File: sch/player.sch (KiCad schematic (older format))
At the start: 74 parts, among them J4 USB_B, U4 CC1101

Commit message: mic add, rf433
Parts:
- removed C28: 1pF, Capacitor_SMD:C_0603_1608Metric_Pad1.05x0.95mm_HandSolder, symbol Device:C
- removed C32: 12pF, Capacitor_SMD:C_0603_1608Metric_Pad1.05x0.95mm_HandSolder, symbol Device:C
- removed C34: 47pF, Capacitor_SMD:C_0603_1608Metric_Pad1.05x0.95mm_HandSolder, symbol Device:C
- removed C?: 220p, symbol Device:C
- removed C?: 10uF, Capacitor_SMD:C_0805_2012Metric, symbol Device:C
- removed D?: 1N5822, Diode_SMD:D_SMA, symbol Diode:1N5822
- removed L1, L2: 12nH, Inductor_SMD:L_0603_1608Metric_Pad1.05x0.95mm_HandSolder, symbol Device:L
- removed L7: 3.3nH, Inductor_SMD:L_0603_1608Metric_Pad1.05x0.95mm_HandSolder, symbol Device:L
- removed R?: 1, symbol Device:R
- removed R?: 18k, symbol Device:R
- removed R?: 11k, symbol Device:R
- removed U?: MC33063AD, Package_SO:SOIC-8_3.9x4.9mm_P1.27mm, symbol Regulator_Switching:MC33063AD
- added BT?: AAA_Cell, symbol Device:Battery_Cell
- added C? (x2): 10uF, Capacitor_SMD:C_0805_2012Metric, symbol Device:C
- added C? (x2): 1uF, Capacitor_SMD:C_0805_2012Metric, symbol Device:C
- added C?: 12pF, Capacitor_SMD:C_0603_1608Metric_Pad1.05x0.95mm_HandSolder, symbol Device:C
- added D?: 1N5822, Diode_SMD:D_SMA, symbol Diode:1N5822
- added D?: ME2149, Package_SO:SO-8_3.9x4.9mm_P1.27mm, symbol native:ME2149
- added J?: AudioJack4, symbol Connector:AudioJack4
- added L?: 4.7mH, Inductor_SMD:L_7.3x7.3_H4.5, symbol Device:L
- added R?: 6k, Resistor_SMD:R_0805_2012Metric, symbol Device:R
- added R? (x2): 1k, Resistor_SMD:R_0805_2012Metric, symbol Device:R
- added R? (x3): 100k, Resistor_SMD:R_0805_2012Metric, symbol Device:R
- added R?: 10k, Resistor_SMD:R_0805_2012Metric, symbol Device:R
- added U?: LM358, symbol Amplifier_Operational:LM358
- C29, C31: value 1.5pF -> 6.8pF
- C30: value 100pF -> 220pF
- C33: value 3.3pF -> 6.8pF
- L3, L4: value 18nH -> 33nH
- L5: value 12nH -> 33nH
- L6: value 12nH -> 18nH
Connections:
- net labels added: ADC_MIC
- net labels removed: VCC
- wire segments 280 -> 323
- no-connect marks 8 -> 9
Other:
- note added: "OLED display"
- note added: "audio frontend\naudio DAC + headphones amp + mic pre amp"
- note added: "power supply"
- note added: "rf frontend\n433 4FSK 10mW"
- moved on the sheet: AE1, C1, C27, C29, C3, C30, C31, C33, C?, D1, D2, J4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

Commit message: schematic almost complete
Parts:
- removed C?: 10uF, Capacitor_SMD:C_0805_2012Metric, symbol Device:C
- removed D1, D?: ME2149, Package_SO:SO-8_3.9x4.9mm_P1.27mm, symbol native:ME2149
- removed R20: 1K5, Resistor_SMD:R_0805_2012Metric_Pad1.15x1.40mm_HandSolder, symbol Device:R
- added C13: 10uF, Capacitor_SMD:C_0805_2012Metric, symbol Device:C
- added C? (x4): 0.1uF, Capacitor_SMD:C_0603_1608Metric_Pad1.05x0.95mm_HandSolder, symbol Device:C
- added D2, D3: 1N5822, Diode_SMD:D_SMA, symbol Diode:1N5822
- added J?: Micro_SD_Card, symbol Connector:Micro_SD_Card
- added Q1: AO3400, TO_SOT_Packages_THT:TO-92_Molded_Narrow, symbol native:AO3400
- added R1, R?: 100k, Resistor_SMD:R_0805_2012Metric, symbol Device:R
- added SW?: RIGHT, symbol Switch:SW_Push
- added SW?: LEFT, symbol Switch:SW_Push
- added SW?: UP, symbol Switch:SW_Push
- added SW?: DN, symbol Switch:SW_Push
- added SW?: volume, symbol Device:RotaryEncoder
- added SW?: call, symbol Switch:SW_Push
- added U2, U5: ME2149, symbol native:ME2149
- added unit 3 of U4
- added U6: XC6206-33, symbol native:XC6206-33
- added Y?: 26M, symbol Device:Crystal
- added Y?: 32768, symbol Device:Crystal
- R2: value 1k -> 33k
- R3: value 6k -> 10k
- R4: renamed from R?; value 1k -> 33k
- R5: renamed from R?; value 6k -> 22k
- gave numbers to parts that had none: 50
- renumbered C3 to C10, C27 to C26, C29 to C31, C30 to C33, C31 to C34, C33 to C36, C1 to C5, D2 to D1, J4 to J1, R10 to R19, R18 to R6, R19 to R7, U4 to U8
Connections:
- net labels added: BAT_DIS, CRG_PWM, DOWN, LEFT, OSC_26M, RF_GPIO, RF_MISO, RF_MOSI, RF_NSS, RF_SCK, RIGHT, R_A, R_B, R_C, SD_MISO, SD_MOSI, SD_NSS, SD_SCK, UP, USB_VBUS, Vbat_FB, call
- net labels removed: MISO, MOSI, NSS, SCK
- wire segments 323 -> 438
- no-connect marks 9 -> 10
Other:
- note added: "D-PAD + \nvolume knob"
- note added: "power supply (BAT DC-DC, VBUS_CHRG)"
- note removed: "power supply"
- moved on the sheet: AE1, BT1, C10, C11, C12, C14, C15, C16, C17, C18, C26, C31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

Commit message: footprints
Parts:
- C1: footprint Capacitor_SMD:C_0603_1608Metric_Pad1.05x0.95mm_HandSolder -> Capacitor_SMD:C_0603_1608Metric
- C10: renamed from C6; footprint Capacitor_SMD:C_0603_1608Metric_Pad1.05x0.95mm_HandSolder -> Capacitor_SMD:C_0603_1608Metric
- C11: renamed from C7; footprint Capacitor_SMD:C_0603_1608Metric_Pad1.05x0.95mm_HandSolder -> Capacitor_SMD:C_0603_1608Metric
- C12: renamed from C8; footprint Capacitor_SMD:C_0603_1608Metric_Pad1.05x0.95mm_HandSolder -> Capacitor_SMD:C_0603_1608Metric
- C13: renamed from C9; footprint Capacitor_SMD:C_0603_1608Metric_Pad1.05x0.95mm_HandSolder -> Capacitor_SMD:C_0603_1608Metric
- C16: renamed from C14; footprint Capacitor_SMD:C_0805_2012Metric -> Capacitor_SMD:C_0603_1608Metric
- C18: renamed from C16; footprint Capacitor_SMD:C_0805_2012Metric -> Capacitor_SMD:C_0603_1608Metric
- C2, C3, C5, C6: renamed from C?; footprint Capacitor_SMD:C_0603_1608Metric_Pad1.05x0.95mm_HandSolder -> Capacitor_SMD:C_0603_1608Metric
- C23: renamed from C26; footprint Capacitor_SMD:C_0603_1608Metric_Pad1.05x0.95mm_HandSolder -> Capacitor_SMD:C_0805_2012Metric
- C24: renamed from C31; footprint Capacitor_SMD:C_0603_1608Metric_Pad1.05x0.95mm_HandSolder -> Capacitor_SMD:C_0805_2012Metric
- C25: renamed from C33; footprint Capacitor_SMD:C_0603_1608Metric_Pad1.05x0.95mm_HandSolder -> Capacitor_SMD:C_0805_2012Metric
- C26: renamed from C34; footprint Capacitor_SMD:C_0603_1608Metric_Pad1.05x0.95mm_HandSolder -> Capacitor_SMD:C_0805_2012Metric
- C27: renamed from C35; footprint Capacitor_SMD:C_0603_1608Metric_Pad1.05x0.95mm_HandSolder -> Capacitor_SMD:C_0805_2012Metric
- C28: renamed from C36; footprint Capacitor_SMD:C_0603_1608Metric_Pad1.05x0.95mm_HandSolder -> Capacitor_SMD:C_0805_2012Metric
- C38: renamed from C29; footprint (none) -> Capacitor_SMD:C_1206_3216Metric
- C39: renamed from C30; footprint (none) -> Capacitor_SMD:C_1206_3216Metric
- C4: renamed from C2; footprint Capacitor_SMD:C_0603_1608Metric_Pad1.05x0.95mm_HandSolder -> Capacitor_SMD:C_0603_1608Metric
- C7: renamed from C3; footprint Capacitor_SMD:C_0603_1608Metric_Pad1.05x0.95mm_HandSolder -> Capacitor_SMD:C_0603_1608Metric
- C8: renamed from C4; footprint Capacitor_SMD:C_0603_1608Metric_Pad1.05x0.95mm_HandSolder -> Capacitor_SMD:C_0603_1608Metric
- L3, L4, L5, L6: footprint Inductor_SMD:L_0603_1608Metric_Pad1.05x0.95mm_HandSolder -> Inductor_SMD:L_0603_1608Metric
- Q1: footprint TO_SOT_Packages_THT:TO-92_Molded_Narrow -> Package_TO_SOT_SMD:SOT-23
- R1: footprint Resistor_SMD:R_0805_2012Metric -> Capacitor_SMD:C_0402_1005Metric
- R10: renamed from R19; footprint Resistor_SMD:R_0805_2012Metric_Pad1.15x1.40mm_HandSolder -> Resistor_SMD:R_0805_2012Metric
- R17: renamed from R15; footprint Resistor_SMD:R_0805_2012Metric -> Capacitor_SMD:C_0402_1005Metric
- R18: renamed from R16; footprint Resistor_SMD:R_0805_2012Metric -> Capacitor_SMD:C_0402_1005Metric
- R2: renamed from R?; footprint Resistor_SMD:R_0805_2012Metric -> Capacitor_SMD:C_0402_1005Metric
- R20: renamed from R18; footprint Resistor_SMD:R_0805_2012Metric -> Capacitor_SMD:C_0402_1005Metric
- R7: renamed from R8; footprint (none) -> Resistor_SMD:R_0805_2012Metric
- R8: renamed from R6; footprint Resistor_SMD:R_0805_2012Metric_Pad1.15x1.40mm_HandSolder -> Capacitor_SMD:C_0402_1005Metric
- R9: renamed from R7; footprint Resistor_SMD:R_0805_2012Metric_Pad1.15x1.40mm_HandSolder -> Capacitor_SMD:C_0402_1005Metric
- SW1, SW2, SW3, SW4, SW5, SW6: renamed from SW?; footprint (none) -> Button_Switch_THT:SW_PUSH_6mm
- U2, U3, U4, U5: footprint (none) -> Package_SO:SSOP-8_3.9x5.05mm_P1.27mm
- U6: footprint (none) -> Package_TO_SOT_SMD:SOT-23
- Y1: renamed from Y?; footprint (none) -> Crystal:Crystal_SMD_5032-2Pin_5.0x3.2mm
- Y2: renamed from Y?; footprint (none) -> Crystal:Crystal_SMD_2012-2Pin_2.0x1.2mm
- gave numbers to parts that had none: 1
- renumbered C10 to C14, C11 to C15, C15 to C17, C17 to C19, C18 to C20, C12 to C21, C13 to C22, C19 to C29, C20 to C30, C21 to C31, C22 to C32, C23 to C33, C24 to C34, C25 to C35, C27 to C36, C28 to C37, C32 to C40, C5 to C9, J2 to J1, J1 to J2, J3 to J4, R9 to R11, R10 to R12, R11 to R13, R12 to R14, R13 to R15, R14 to R16, R17 to R19, R20 to R21, R2 to R3, R3 to R4, R4 to R5, R5 to R6, U8 to U7, U7 to U8
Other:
- moved on the sheet: C16, C17, C18, C19, C20, J1, J3, R7, SW1, SW2, SW3, SW4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

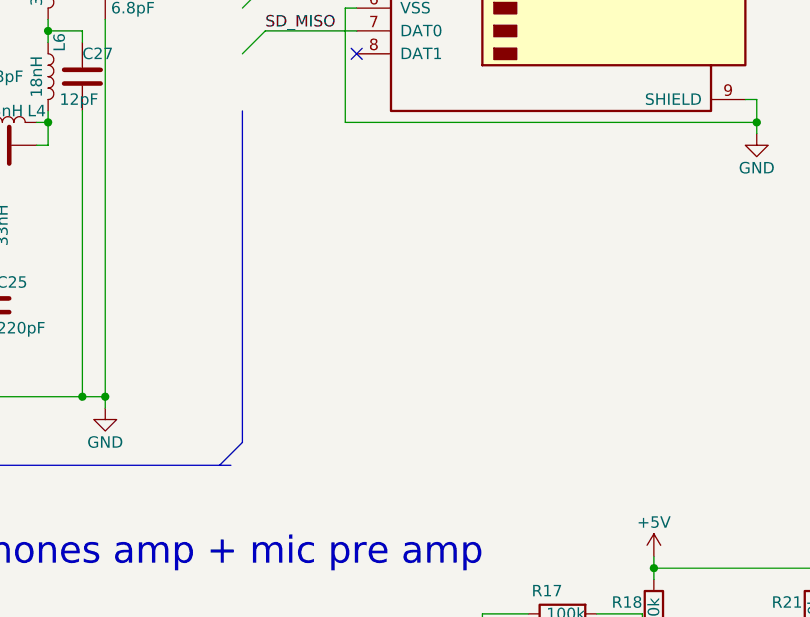
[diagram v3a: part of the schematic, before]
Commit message: 5807 FM sch add
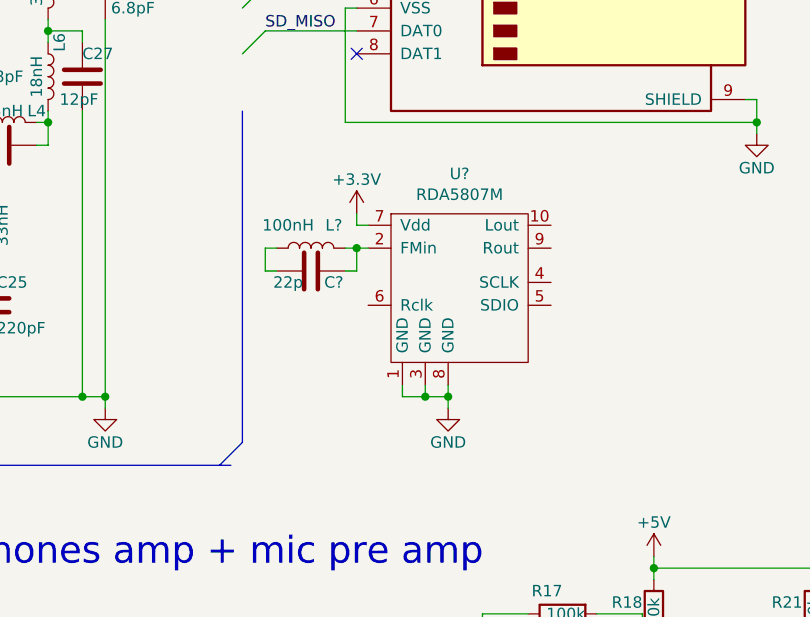
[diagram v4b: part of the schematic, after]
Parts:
- added C?: 22p, symbol Device:C
- added L?: 100nH, symbol Device:L
- added U?: RDA5807M, symbol native:RDA5807M
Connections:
- wire segments 438 -> 453
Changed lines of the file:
@@
 Wire Bus Line
 	8050 1950 8050 3400
+$Comp
+L native:RDA5807M U?
+U 1 1 61D26FB3
+P 9000 2600
+F 0 "U?" H 9000 2975 50  0000 C CNN
+F 1 "RDA5807M" H 9000 2884 50  0000 C CNN
+F 2 "" H 9000 2550 50  0001 C CNN
+F 3 "" H 9000 2550 50  0001 C CNN
+	1    9000 2600
+	1    0    0    -1
+$EndComp
+$Comp
+L power:+3.3V #PWR?
+U 1 1 61D2DFC9
+P 8550 2400
+F 0 "#PWR?" H 8550 2250 50  0001 C CNN
+F 1 "+3.3V" H 8550 2550 50  0000 C CNN
+F 2 "" H 8550 2400 50  0001 C CNN
+F 3 "" H 8550 2400 50  0001 C CNN
+	1    8550 2400
+	1    0    0    -1
+$EndComp
+Wire Wire Line
+	8550 2400 8550 2450
+Wire Wire Line
+	8550 2450 8600 2450
+$Comp
+L power:GND #PWR?
+U 1 1 61D72BB2
+P 8950 3250
+F 0 "#PWR?" H 8950 3000 50  0001 C CNN
+F 1 "GND" H 8950 3100 50  0000 C CNN
+F 2 "" H 8950 3250 50  0001 C CNN
+F 3 "" H 8950 3250 50  0001 C CNN
+	1    8950 3250
+	1    0    0    -1
+$EndComp
+Wire Wire Line
+	8750 3150 8750 3200
+Wire Wire Line
+	8750 3200 8850 3200
+Wire Wire Line
+	8850 3200 8850 3150
+Wire Wire Line
+	8850 3200 8950 3200
+Wire Wire Line
+	8950 3200 8950 3150
+Connection ~ 8850 3200
+Wire Wire Line
+	8950 3250 8950 3200
+Connection ~ 8950 3200
+$Comp
+L Device:L L?
+U 1 1 61E7B564
+P 8350 2550
+F 0 "L?" V 8450 2450 50  0000 C CNN
+F 1 "100nH" V 8450 2650 50  0000 C CNN
+F 2 "" H 8350 2550 50  0001 C CNN
+F 3 "~" H 8350 2550 50  0001 C CNN
+	1    8350 2550
+	0    -1   -1   0
+$EndComp
+$Comp
+L Device:C C?
+U 1 1 61E7C3A6
+P 8350 2650
+F 0 "C?" V 8300 2550 50  0000 C CNN
+F 1 "22p" V 8300 2750 50  0000 C CNN
+F 2 "" H 8388 2500 50  0001 C CNN
+F 3 "~" H 8350 2650 50  0001 C CNN
+	1    8350 2650
+	0    -1   -1   0
+$EndComp
+Wire Wire Line
+	8600 2550 8550 2550
+Wire Wire Line
+	8550 2550 8550 2650
+Wire Wire Line
+	8550 2650 8500 2650
+Connection ~ 8550 2550
+Wire Wire Line
+	8550 2550 8500 2550
+Wire Wire Line
+	8200 2550 8150 2550
+Wire Wire Line
+	8150 2550 8150 2650
+Wire Wire Line
+	8150 2650 8200 2650
 Wire Bus Line
 	5200 3500 8000 3500

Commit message: sch ok
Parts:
- added C?: 0.1uF, Capacitor_SMD:C_0603_1608Metric, symbol Device:C
- added C? (x2): 22p, symbol Device:C
- added J?: SWD, symbol Connector_Generic:Conn_01x03
- added Q?: AO3400, Package_TO_SOT_SMD:SOT-23, symbol native:AO3400
- added Q?: 2SC3583, Package_TO_SOT_THT:TO-92_Inline, symbol Transistor_BJT:2SC1815
- added R? (x3): 100k, Capacitor_SMD:C_0402_1005Metric, symbol Device:R
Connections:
- net labels added: ANT, ANT_IN, PA_ANT, RDA_CLK, RDA_L, RDA_R, RDA_SCL, RDA_SDA, SWCLK, SWDIO
- wire segments 453 -> 506
- no-connect marks 10 -> 13
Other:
- moved on the sheet: C34, C35, C36, C37, C38, C39, C40, J2, J4, R17, R18, R19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

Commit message: rda registers
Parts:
- removed U9: LM4811, Package_SO:TSSOP-10_3x3mm_P0.5mm, symbol Amplifier_Audio:LM4811
- added U9: LM4810, Package_SO:TSSOP-8_3x3mm_P0.65mm, symbol Amplifier_Audio:LM4810
- C1, C10, C11, C12, C13, C16, C18, C2, C3, C4, C5, C6, C7, C8: footprint Capacitor_SMD:C_0603_1608Metric -> Capacitor_SMD:C_0402_1005Metric
- C41: renamed from C?; footprint Capacitor_SMD:C_0603_1608Metric -> Capacitor_SMD:C_0402_1005Metric
- C42, C43, C44: renamed from C?; footprint (none) -> Capacitor_SMD:C_0402_1005Metric
- J2: footprint Connector_Wire:SolderWire-0.127sqmm_1x05_P3.7mm_D0.48mm_OD1mm -> Connector_USB:USB_Micro-B_Molex_47346-0001
- L7: renamed from L?; footprint (none) -> Inductor_SMD:L_0603_1608Metric
- Q3: renamed from Q?; footprint Package_TO_SOT_THT:TO-92_Inline -> Package_TO_SOT_SMD:SOT-23
- U10: renamed from U?; footprint (none) -> Package_SO:MSOP-10_3x3mm_P0.5mm
- U8: footprint DBQ16 -> Package_SO:SSOP-16_3.9x4.9mm_P0.635mm
- gave numbers to parts that had none: 5
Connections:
- net +5V: now also U9.8 (VDD)
- net GND: now also U9.4 (GND)
- net at C38.1: now also U9.1 (VOUT1)
- net at C34.1: now also U9.2 (VIN1)
- net at C36.2: now also U9.3 (BYPASS)
- net at C35.1: now also U9.6 (VIN2)
- net at C39.1: now also U9.7 (VOUT2)
- new net SND_ON: U9.5 (SHDN)

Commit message: add micro and audio checked
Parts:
- removed C38, C39: 100uF, Capacitor_SMD:C_1206_3216Metric, symbol Device:C_Polarized
- removed SW2: volume, Button_Switch_THT:SW_PUSH_6mm, symbol Device:RotaryEncoder
- added C38, C39: 100uF, Capacitor_SMD:C_1206_3216Metric, symbol Device:CP
- added C45: 1uF, Capacitor_SMD:C_0805_2012Metric, symbol Device:C
- added MK1: Mic, Capacitor_THT:CP_Radial_D5.0mm_P2.50mm, symbol Device:Microphone_Condenser
- added Q4: AO3400, Package_TO_SOT_SMD:SOT-23, symbol native:AO3400
- added R25: 100k, Resistor_SMD:R_0402_1005Metric, symbol Device:R
- added R26, R27: 33R, Resistor_SMD:R_0402_1005Metric, symbol Device:R
- added R28, R29, R30, R31, R32, R33: 10k, Resistor_SMD:R_0402_1005Metric, symbol Device:R
- added SW2: volume, local:mouse_encoder, symbol Device:Rotary_Encoder
- BT1: footprint (none) -> Connector_PinHeader_2.54mm:PinHeader_2x01_P2.54mm_Vertical
- C15: footprint Capacitor_SMD:C_0603_1608Metric_Pad1.05x0.95mm_HandSolder -> Capacitor_SMD:C_0805_2012Metric
- C23: footprint Capacitor_SMD:C_0805_2012Metric -> Capacitor_SMD:C_0402_1005Metric
- C24, C25, C26, C27, C28: footprint Capacitor_SMD:C_0805_2012Metric -> Capacitor_SMD:C_0603_1608Metric
- C29, C30: value 68nF -> 0.33uF; footprint Capacitor_SMD:C_0805_2012Metric -> Capacitor_SMD:C_0603_1608Metric
- C32, C33: value 1nF -> 470p; footprint Capacitor_SMD:C_0805_2012Metric -> Capacitor_SMD:C_0603_1608Metric
- J1: footprint (none) -> local:display_14p
- J3: footprint (none) -> Connector_Card:microSD_HC_Hirose_DM3BT-DSF-PEJS
- J4: footprint (none) -> Connector_Audio:Jack_3.5mm_PJ320D_Horizontal
- J5: footprint (none) -> local:3WIRE_PADS
- L2: footprint Inductor_SMD:L_7.3x7.3_H4.5 -> Inductor_SMD:L_1206_3216Metric
- R1, R2, R20, R22, R23, R24, R8, R9: footprint Capacitor_SMD:C_0402_1005Metric -> Resistor_SMD:R_0402_1005Metric
- R10, R21, R4: footprint Resistor_SMD:R_0805_2012Metric -> Resistor_SMD:R_0402_1005Metric
- R11, R12, R13, R14: value 680 -> 33R; footprint Resistor_SMD:R_0805_2012Metric -> Resistor_SMD:R_0402_1005Metric
- R15, R16: value 1,5k -> 10k; footprint Resistor_SMD:R_0805_2012Metric -> Resistor_SMD:R_0402_1005Metric
- U7: footprint belkin:cc1101 -> local:cc1101
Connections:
- net +5V: now also R33.1
- net GND: now also J4.R2, U7.3 (GDO2), U8.5 (NC), MK1.2 (+), R25.2; no longer J4.T
- net RDA_L: now also R26.1; no longer C33.2, C35.2, R14.1, U3.7
- net RDA_R: now also R27.2; no longer C32.2, C34.2, R13.1, U3.1
- net R_A: now also SW2.A
- net R_B: now also SW2.B
- net R_C: now also SW2.C
- net at U8.7 (VOUTL): now also R11.1, R26.2; no longer R12.1
- net at U8.8 (VOUTR): now also R12.1, R27.1; no longer R11.1
- net MIC_ON: now reaches U1.35 (PB14)
- net MIC_ON: now also R32.1
- net at C40.2, R21.2: now also J4.S; no longer J4.R1
- net at U9.7 (VOUT2): now also C39.1, R31.2
- net at U9.1 (VOUT1): now also C38.1, R30.2
- net at C34.1: now also R28.1; no longer U9.2 (VIN1)
- net at C35.1: now also R29.1; no longer U9.6 (VIN2)
- net at C40.1, R19.2: now also C45.1
- new net: C32.2, C34.2, R13.1, U3.1
- new net: C33.2, C35.2, R14.1, U3.7
- new net: C38.2, J4.R1
- new net: C39.2, J4.T
- new net: R28.2, R30.1, U9.2 (VIN1)
- new net: R29.2, R31.1, U9.6 (VIN2)
- new net: C45.2, MK1.1 (-), Q4.2 (S)
- new net: Q4.1 (G), R25.1, R32.2
- new net: Q4.3 (D), R33.2
- no-connect marks 13 -> 10
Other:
- moved on the sheet: C29, C30, C31, C32, C33, C34, C35, R11, R12, R13, R14, R15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
